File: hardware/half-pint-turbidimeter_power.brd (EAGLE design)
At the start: 17 x 31 mm, 19 parts, among them U1 MCP73831

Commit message: minor edits to eagle schematics
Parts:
- removed D11: RED, SparkFun:LED-0603
- removed JP2: STAND-OFF, SparkFun:STAND-OFF
- removed R330: 330, SparkFun:0402-RES
- added D2: GREEN, SparkFun:LED-0603
- added FRAME1: FRAME-LETTER, SparkFun-Aesthetics:CREATIVE_COMMONS
- added R2: R330, SparkFun:0402-RES
- added U$1: (no value), SparkFun-Aesthetics:CREATIVE_COMMONS
- D1: value GREEN -> RED
- R3: value 2K -> R2K
- moved D1 4.57 mm to (2.79, 17.8)
- moved R1 3.30 mm to (4.06, 17.8)
- renumbered R2K to R3
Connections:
- net GND: now also D2.C; no longer D1.C
- net N$2: now also D2.A, R2.2; no longer D1.A, R1.2
- net N$3: now also D1.A, R1.1; no longer D11.A, R330.1
- net STAT: now also D1.C, R2.1; no longer D11.C, R1.1
- net VIN: now also R1.2; no longer R330.2
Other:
- board text added: "AWQUA"
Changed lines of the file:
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@@
 v2.0  2016/02/22
 github.com/awqua</text>
+<text x="18.542" y="-11.176" size="1.778" layer="25">AWQUA</text>
 </plain>
 <attributes>
@@
 </autorouter>
 <elements>
-<element name="D11" library="SparkFun" package="LED-0603" value="RED" x="2.794" y="17.78" smashed="yes" rot="R180">
+<element name="D1" library="SparkFun" package="LED-0603" value="RED" x="2.794" y="17.78" smashed="yes" rot="R180">
 <attribute name="VALUE" x="3.1115" y="15.24" size="0.4064" layer="25" rot="R90"/>
 </element>
-<element name="R330" library="SparkFun" package="0402-RES" value="330" x="4.064" y="17.78" smashed="yes" rot="R270">
+<element name="R1" library="SparkFun" package="0402-RES" value="R330" x="4.064" y="17.78" smashed="yes" rot="R270">
 <attribute name="NAME" x="5.08" y="17.018" size="0.4064" layer="25" font="vector" rot="R90"/>
 </element>
@@
 <attribute name="VALUE" x="10.0965" y="23.6855" size="0.4064" layer="25" rot="R90"/>
 </element>
-<element name="R2K" library="SparkFun" package="0402-RES" value="2K" x="10.16" y="22.606" smashed="yes">
+<element name="R3" library="SparkFun" package="0402-RES" value="R2K" x="10.16" y="22.606" smashed="yes">
 <attribute name="NAME" x="9.398" y="21.59" size="0.4064" layer="25" font="vector"/>
 </element>
-<element name="JP2" library="SparkFun" package="STAND-OFF" value="STAND-OFF" x="15.748" y="27.432"/>
 <element name="C3" library="SparkFun" package="0402-CAP" value="4.7uF" x="11.176" y="29.718" smashed="yes">
 <attribute name="VALUE" x="9.8425" y="30.353" size="0.4064" layer="25"/>
@@
 </element>
 <element name="2.2UF" library="SparkFun-Passives" package="0603-CAP" value="" x="15.494" y="9.652"/>
-<element name="R1" library="SparkFun" package="0402-RES" value="R330" x="4.064" y="14.478" smashed="yes" rot="R270">
+<element name="R2" library="SparkFun" package="0402-RES" value="R330" x="4.064" y="14.478" smashed="yes" rot="R270">
 <attribute name="VALUE" x="5.207" y="13.6525" size="0.4064" layer="25" rot="R90"/>
 </element>
-<element name="D1" library="SparkFun" package="LED-0603" value="GREEN" x="2.794" y="13.208" smashed="yes" rot="R180">
+<element name="D2" library="SparkFun" package="LED-0603" value="GREEN" x="2.794" y="13.208" smashed="yes" rot="R180">
 <attribute name="VALUE" x="3.1115" y="9.906" size="0.4064" layer="25" rot="R90"/>
 </element>
@@
 <element name="U$3" library="awqua_eagle_library" package="USBMICRO-DX4R005JJ2" value="USBMICRO-DX4R005JJ2" x="1.778" y="25.4" rot="R270"/>
 <element name="JP3" library="SparkFun" package="STAND-OFF" value="STAND-OFF" x="15.748" y="20.828"/>
+<element name="U$1" library="SparkFun-Aesthetics" package="CREATIVE_COMMONS" value="" x="-12.7" y="-10.922"/>
+<element name="FRAME1" library="SparkFun-Aesthetics" package="CREATIVE_COMMONS" value="FRAME-LETTER" x="-12.7" y="-19.558"/>
 </elements>
 <signals>
 <signal name="GND">
 <contactref element="U1" pad="2"/>
-<contactref element="R2K" pad="2"/>
+<contactref element="R3" pad="2"/>
 <contactref element="C3" pad="2"/>
 <contactref element="C4" pad="2"/>
@@
 <vertex x="1.778" y="-0.508"/>
 <vertex x="1.778" y="30.988"/>
-<vertex x="31.242" y="31.242"/>
-<vertex x="31.242" y="-0.254"/>
+<vertex x="19.812" y="31.496"/>
+<vertex x="19.812" y="0"/>
 </polygon>
 <polygon width="0.254" layer="1" isolate="0.3048">
 <vertex x="1.778" y="30.988"/>
-<vertex x="30.734" y="31.242"/>
-<vertex x="30.734" y="-0.508"/>
+<vertex x="19.558" y="31.496"/>
+<vertex x="19.558" y="-0.254"/>
 <vertex x="1.778" y="-0.762"/>
 </polygon>
@@
 <contactref element="+OUT-" pad="2"/>
 <contactref element="OPT_10NF" pad="2"/>
-<contactref element="D1" pad="C"/>
+<contactref element="D2" pad="C"/>
 <contactref element="U$3" pad="GND"/>
 <contactref element="U$3" pad="HOLE1"/>
@@
 </signal>
 <signal name="N$3">
-<contactref element="D11" pad="A"/>
-<contactref element="R330" pad="1"/>
+<contactref element="D1" pad="A"/>
+<contactref element="R1" pad="1"/>
 <wire x1="4.064" y1="18.4912" x2="2.8448" y2="18.4912" width="0.3048" layer="1"/>
 <wire x1="2.8448" y1="18.4912" x2="2.794" y2="18.53" width="0.2032" layer="1"/>
@@
 <signal name="PROG">
 <contactref element="U1" pad="5"/>
-<contactref element="R2K" pad="1"/>
+<contactref element="R3" pad="1"/>
 <wire x1="9.3472" y1="23.5712" x2="9.3472" y2="22.7584" width="0.2032" layer="1"/>
 <wire x1="8.7376" y1="24.1808" x2="9.3472" y2="23.5712" width="0.2032" layer="1"/>
@@
 </signal>
 <signal name="STAT">
-<contactref element="D11" pad="C"/>
+<contactref element="D1" pad="C"/>
 <contactref element="U1" pad="1"/>
-<contactref element="R1" pad="1"/>
+<contactref element="R2" pad="1"/>
 <wire x1="4.064" y1="15.128" x2="3.922" y2="15.128" width="0.3048" layer="1"/>
 <wire x1="3.922" y1="15.128" x2="2.794" y2="16.256" width="0.3048" layer="1"/>
@@
 </signal>
 <signal name="VIN">
-<contactref element="R330" pad="2"/>
+<contactref element="R1" pad="2"/>
 <contactref element="U1" pad="4"/>
 <contactref element="C3" pad="1"/>
@@
 </signal>
 <signal name="N$2">
-<contactref element="R1" pad="2"/>
-<contactref element="D1" pad="A"/>
+<contactref element="R2" pad="2"/>
+<contactref element="D2" pad="A"/>
 <wire x1="4.064" y1="14.0208" x2="2.8448" y2="14.0208" width="0.3048" layer="1"/>
 <wire x1="2.8448" y1="14.0208" x2="2.794" y2="13.958" width="0.2032" layer="1"/>

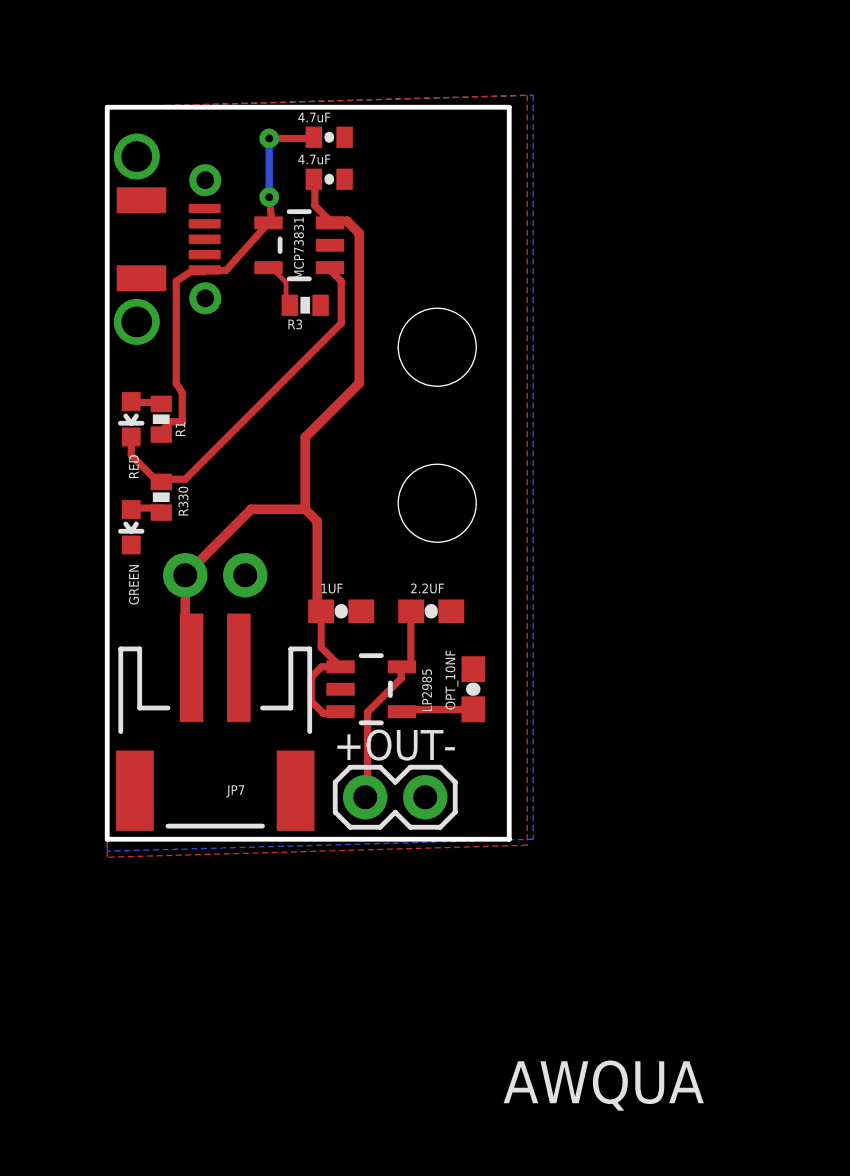
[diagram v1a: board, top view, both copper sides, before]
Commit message: added voltage protection diode
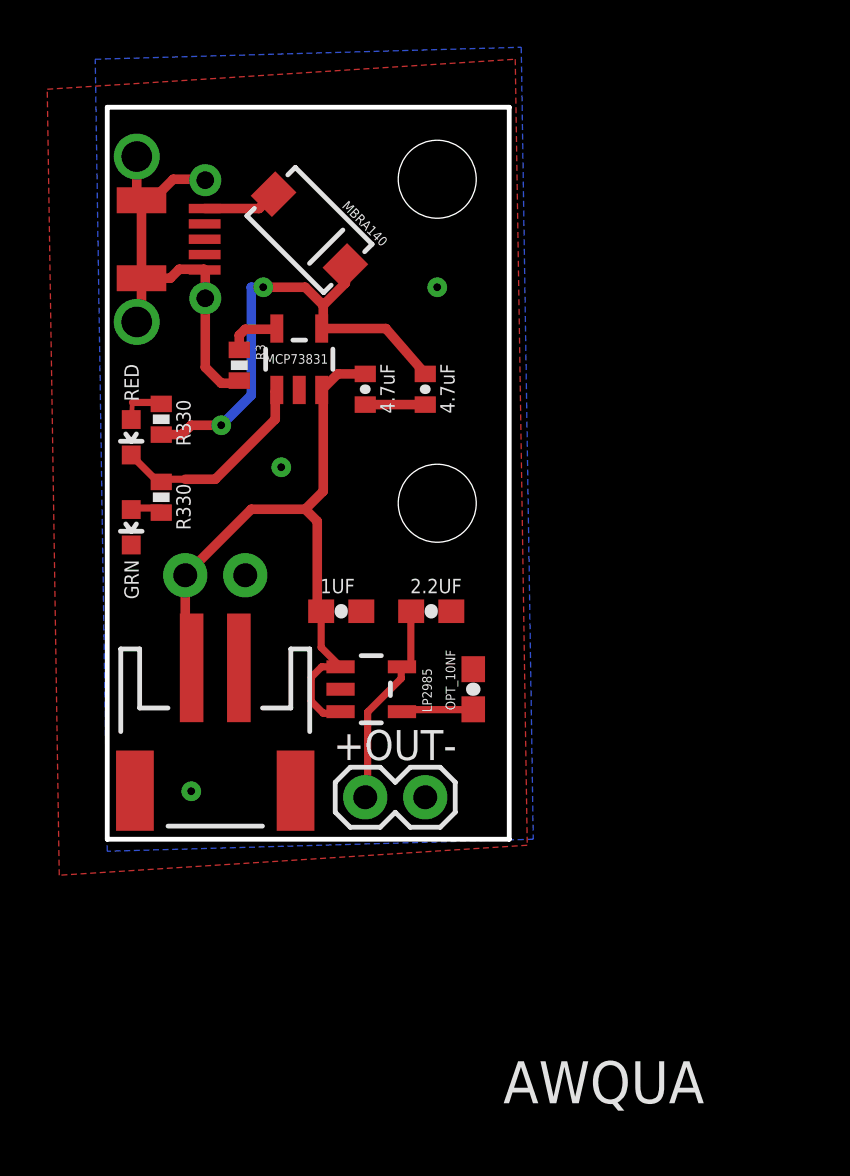
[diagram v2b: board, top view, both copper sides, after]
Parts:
- added D3: MBRA140, SparkFun-DiscreteSemi:SMA-DIODE
- D2: value GREEN -> GRN
- moved C3 11.4 mm to (15.2, 19.1), turned to 270 degrees
- moved C4 9.02 mm to (12.7, 19.1), turned to 270 degrees
- moved JP3 7.11 mm to (15.7, 27.9)
- moved U1 4.83 mm to (9.91, 20.3), turned to 0 degrees
- moved R3 3.78 mm to (7.37, 20.1), turned to 270 degrees
- moved D1 0.76 mm to (2.79, 17.0)
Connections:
- new net N$5: D3.A, U$3.GND
- net GND: now also U$3.VCC; no longer U$3.GND
- net VIN: now also D3.C; no longer U$3.VCC
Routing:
- net GND: track 0.00 -> 21.5 mm
- net VCC: track 37.7 -> 29.0 mm
- net STAT: track 15.5 -> 9.04 mm
- net N$5: track 0.00 -> 3.17 mm
- net VIN: track 17.8 -> 20.8 mm
- net N$3: track 1.34 -> 2.01 mm
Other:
- board text added: "awqua power supply v2.0.1 2016/04/06 github.com/awqua"
- board text removed: "awqua power supply v2.0 2016/02/22 github.com/awqua"

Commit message: minor edits
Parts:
- moved D3 1.05 mm to (10.1, 26.8)
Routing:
- net VIN: track 20.8 -> 21.7 mm
- net N$5: track 3.17 -> 3.79 mm
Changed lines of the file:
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@@
 <element name="U$1" library="SparkFun-Aesthetics" package="CREATIVE_COMMONS" value="" x="-12.7" y="-10.922"/>
 <element name="FRAME1" library="SparkFun-Aesthetics" package="CREATIVE_COMMONS" value="FRAME-LETTER" x="-12.7" y="-19.558"/>
-<element name="D3" library="SparkFun-DiscreteSemi" package="SMA-DIODE" value="MBRA140" x="10.33960625" y="25.790028125" smashed="yes" rot="R315">
-<attribute name="PROD_ID" value="DIO-08053" x="10.33960625" y="25.790028125" size="1.778" layer="27" rot="R315" display="off"/>
-<attribute name="VALUE" x="11.68664375" y="26.77785625" size="0.4064" layer="25" rot="R315"/>
+<element name="D3" library="SparkFun-DiscreteSemi" package="SMA-DIODE" value="MBRA140" x="10.08560625" y="26.806028125" smashed="yes" rot="R315">
+<attribute name="PROD_ID" value="DIO-08053" x="10.08560625" y="26.806028125" size="1.778" layer="27" rot="R315" display="off"/>
+<attribute name="VALUE" x="11.43264375" y="27.79385625" size="0.4064" layer="25" rot="R315"/>
 </element>
 </elements>
@@
 <contactref element="R1" pad="2"/>
 <contactref element="D3" pad="C"/>
-<wire x1="11.859884375" y1="24.269746875" x2="11.859884375" y2="23.543884375" width="0.4064" layer="1"/>
-<wire x1="11.859884375" y1="23.543884375" x2="10.922" y2="22.606" width="0.4064" layer="1"/>
+<wire x1="11.605884375" y1="25.285746875" x2="10.922" y2="24.559884375" width="0.4064" layer="1"/>
+<wire x1="10.922" y1="24.559884375" x2="10.922" y2="22.606" width="0.4064" layer="1"/>
 <wire x1="10.922" y1="22.606" x2="10.922" y2="21.6861" width="0.4064" layer="1"/>
 <wire x1="10.922" y1="21.6861" x2="10.856" y2="21.6201" width="0.4064" layer="1"/>
@@
 <contactref element="D3" pad="A"/>
 <contactref element="U$3" pad="GND"/>
-<wire x1="5.903" y1="26.7" x2="8.20901875" y2="26.7" width="0.4064" layer="1"/>
-<wire x1="8.20901875" y1="26.7" x2="8.819325" y2="27.31030625" width="0.4064" layer="1"/>
+<wire x1="5.903" y1="26.7" x2="7.95501875" y2="26.7" width="0.4064" layer="1"/>
+<wire x1="7.95501875" y1="26.7" x2="8.565325" y2="28.32630625" width="0.4064" layer="1"/>
 </signal>
 <signal name="N$6">
